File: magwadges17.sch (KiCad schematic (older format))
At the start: 23 parts, among them J1 CONN_02X03, J2 JACK_2P, Q1 BC846BDW1, Q2 BC846BDW1, U1 ATTINY2313-20MU, U2 FT25H16

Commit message: Updated schematic
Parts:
- removed D1, D2, D3, D4: LED, custom:LTST-C230KRKT, symbol LED
- removed Q1, Q2: BC846BDW1, TO_SOT_Packages_SMD:SOT-363_SC-70-6, symbol BC846BDW1
- removed R1, R2: 47, Resistors_SMD:R_0805, symbol R
- removed R3: 1K, Resistors_SMD:R_0805, symbol R
- removed R4, R5: 1M, Resistors_SMD:R_0805, symbol R
- removed R6, R7: 2K2, Resistors_SMD:R_0805, symbol R
- removed U1: ATTINY2313-20MU, Housings_DFN_QFN:QFN-20-1EP_4x4mm_Pitch0.5mm, symbol ATTINY2313-20MU
- removed U2: FT25H16, Housings_SOIC:SOIC-8_3.9x4.9mm_Pitch1.27mm, symbol FT25H16
- added RN1: R_Pack04, symbol R_Pack04
- added S5, S6, S7, S8: SW_SPST, custom:PTS645, symbol SW_SPST
- added U1: ATTINY861A-MU, QFN_MLF32, symbol ATTINY861A-MU
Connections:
- net labels added: SW_A, SW_B, SW_C, SW_D, SW_E, SW_F, SW_G, SW_H, TouchC
- wire segments 93 -> 66
- no-connect marks 8 -> 0
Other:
- moved on the sheet: J1, S1, S2, S3, S4

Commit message: Updated schematic
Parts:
- removed U1: ATTINY861A-MU, QFN_MLF32, symbol ATTINY861A-MU
- added U?: ATTINY861A-SU, Housings_SOIC:SOIC-20W_7.5x12.8mm_Pitch1.27mm, symbol ATTINY861A-SU
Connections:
- net GND: now also U?.16 (AGND), U?.6 (GND)
- net SW_A: now also U?.17 ((AREF/PCINT3)PA3)
- net SW_B: now also U?.14 ((ADC3/ICP0/PCINT4)PA4)
- net SW_C: now also U?.13 ((ADC4/AIN2/PCINT5)PA5)
- net SW_D: now also U?.12 ((ADC5/AIN0/PCINT6)PA6)
- net SW_E: now also U?.11 ((ADC6/AIN1/PCINT7)PA7)
- net SW_F: now also U?.7 ((ADC7/~OC1D~/CLKI/XTAL1/PCINT12)PB4)
- net SW_G: now also U?.8 ((ADC8/OC1D/CLKO/XTAL2/PCINT13)PB5)
- net SW_H: now also U?.9 ((ADC9/INT0/T0/PCINT14)PB6)
- net TouchA: now also U?.20 ((ADC0/DI/SDA/PCINT0)PA0)
- net TouchB: now also U?.19 ((ADC1/DO/PCINT1)PA1)
- net TouchC: now also U?.18 ((ADC2/INT1/USCK/SCL/PCINT2)PA2)
- net VCC: now also U?.15 (AVCC), U?.5 (VCC)
- net reset: now also U?.10 ((ADC10/~RESET~/PCINT15)PB7)
- net at J2.2, J2.3, LS1.1: now also U?.4 ((OC1B/PCINT11)PB3)
- net at J1.1 (P1): now also U?.2 ((MISO/DO/OC1A/PCINT9)PB1)
- net at J1.3 (P3): now also U?.3 ((SCK/USCK/SCL/~OC1B~/PCINT10)PB2)
- net at J1.4 (P4): now also U?.1 ((MOSI/DI/SDA/~OC1A~/PCINT8)PB0)
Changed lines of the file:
@@
 Wire Wire Line
 	7750 5250 7750 5200
-$Comp
-L ATTINY861A-MU U1
-U 1 1 597BCA60
-P 4050 2050
-F 0 "U1" H 3150 3000 50  0000 C CNN
-F 1 "ATTINY861A-MU" H 4750 1100 50  0000 C CNN
-F 2 "QFN_MLF32" H 4050 2050 50  0001 C CIN
-F 3 "" H 4050 2050 50  0001 C CNN
-	1    4050 2050
-	1    0    0    -1
-$EndComp
 Wire Wire Line
 	6400 3500 6350 3500
@@
 Wire Wire Line
 	7250 2050 7900 2050
+$Comp
+L ATTINY861A-SU U?
+U 1 1 597BFFA6
+P 4050 2050
+F 0 "U?" H 3150 3000 50  0000 C CNN
+F 1 "ATTINY861A-SU" H 4800 1100 50  0000 C CNN
+F 2 "Housings_SOIC:SOIC-20W_7.5x12.8mm_Pitch1.27mm" H 4050 2050 50  0001 C CIN
+F 3 "" H 4050 2050 50  0001 C CNN
+	1    4050 2050
+	1    0    0    -1
+$EndComp
 $EndSCHEMATC

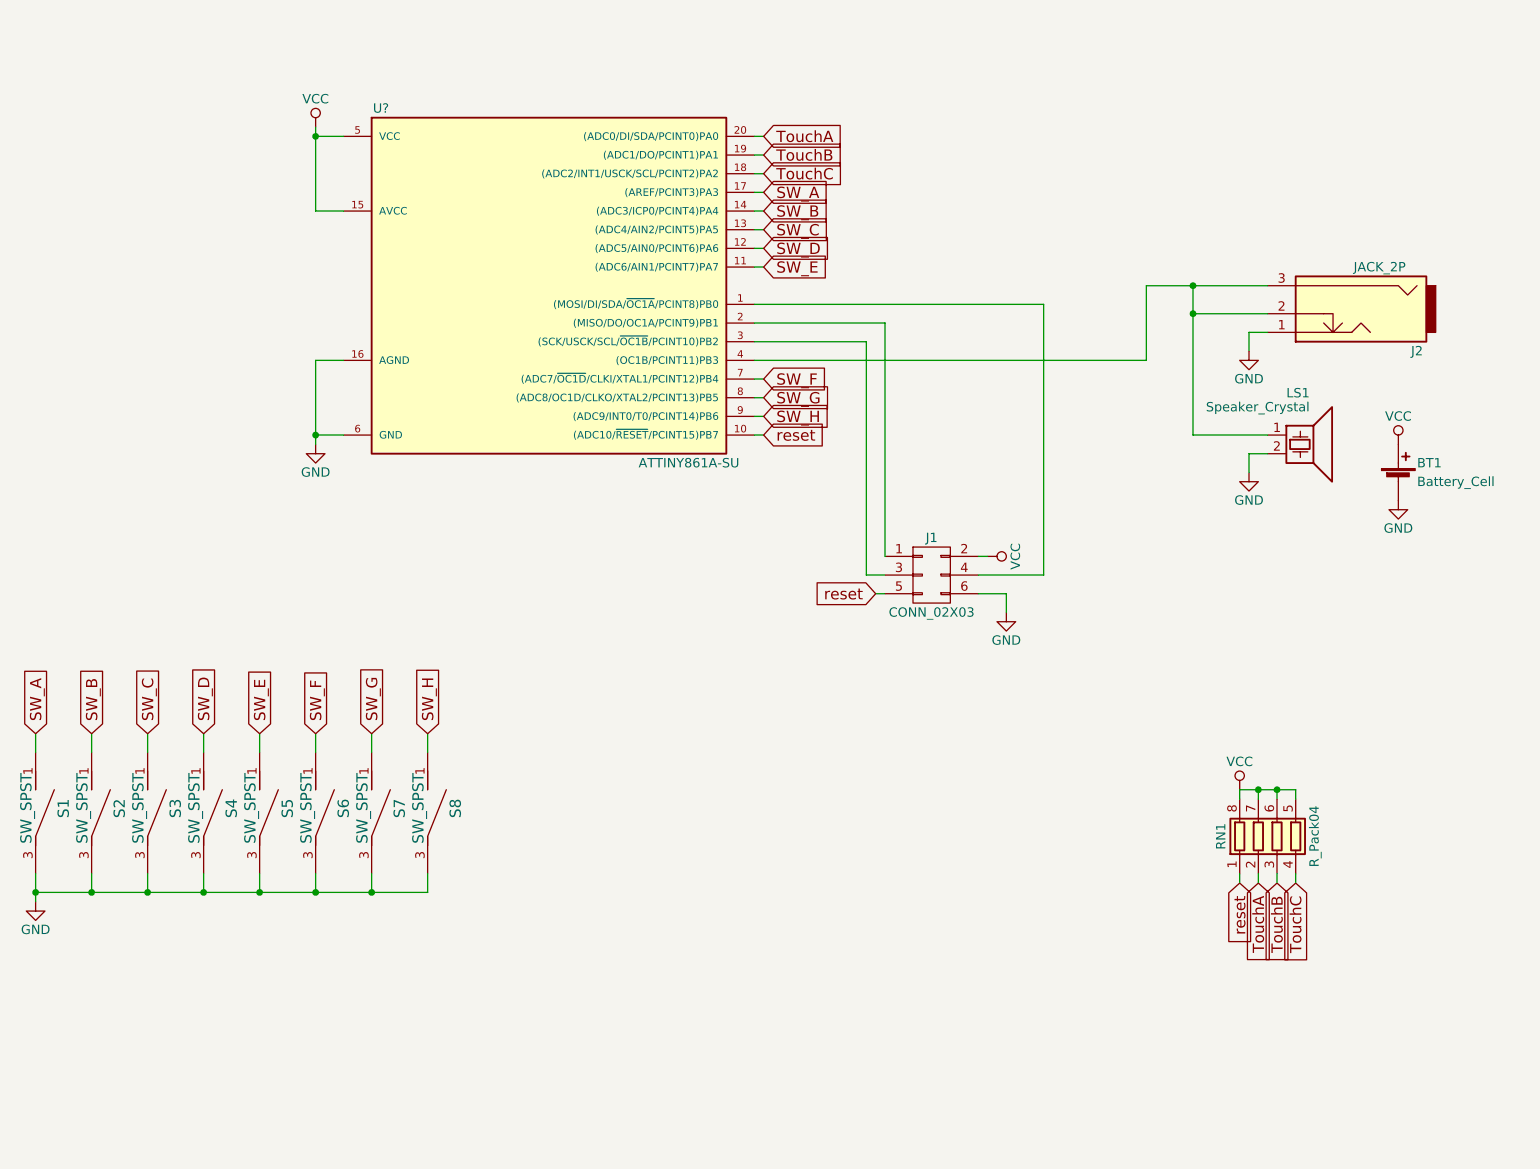
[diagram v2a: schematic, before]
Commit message: single layer in
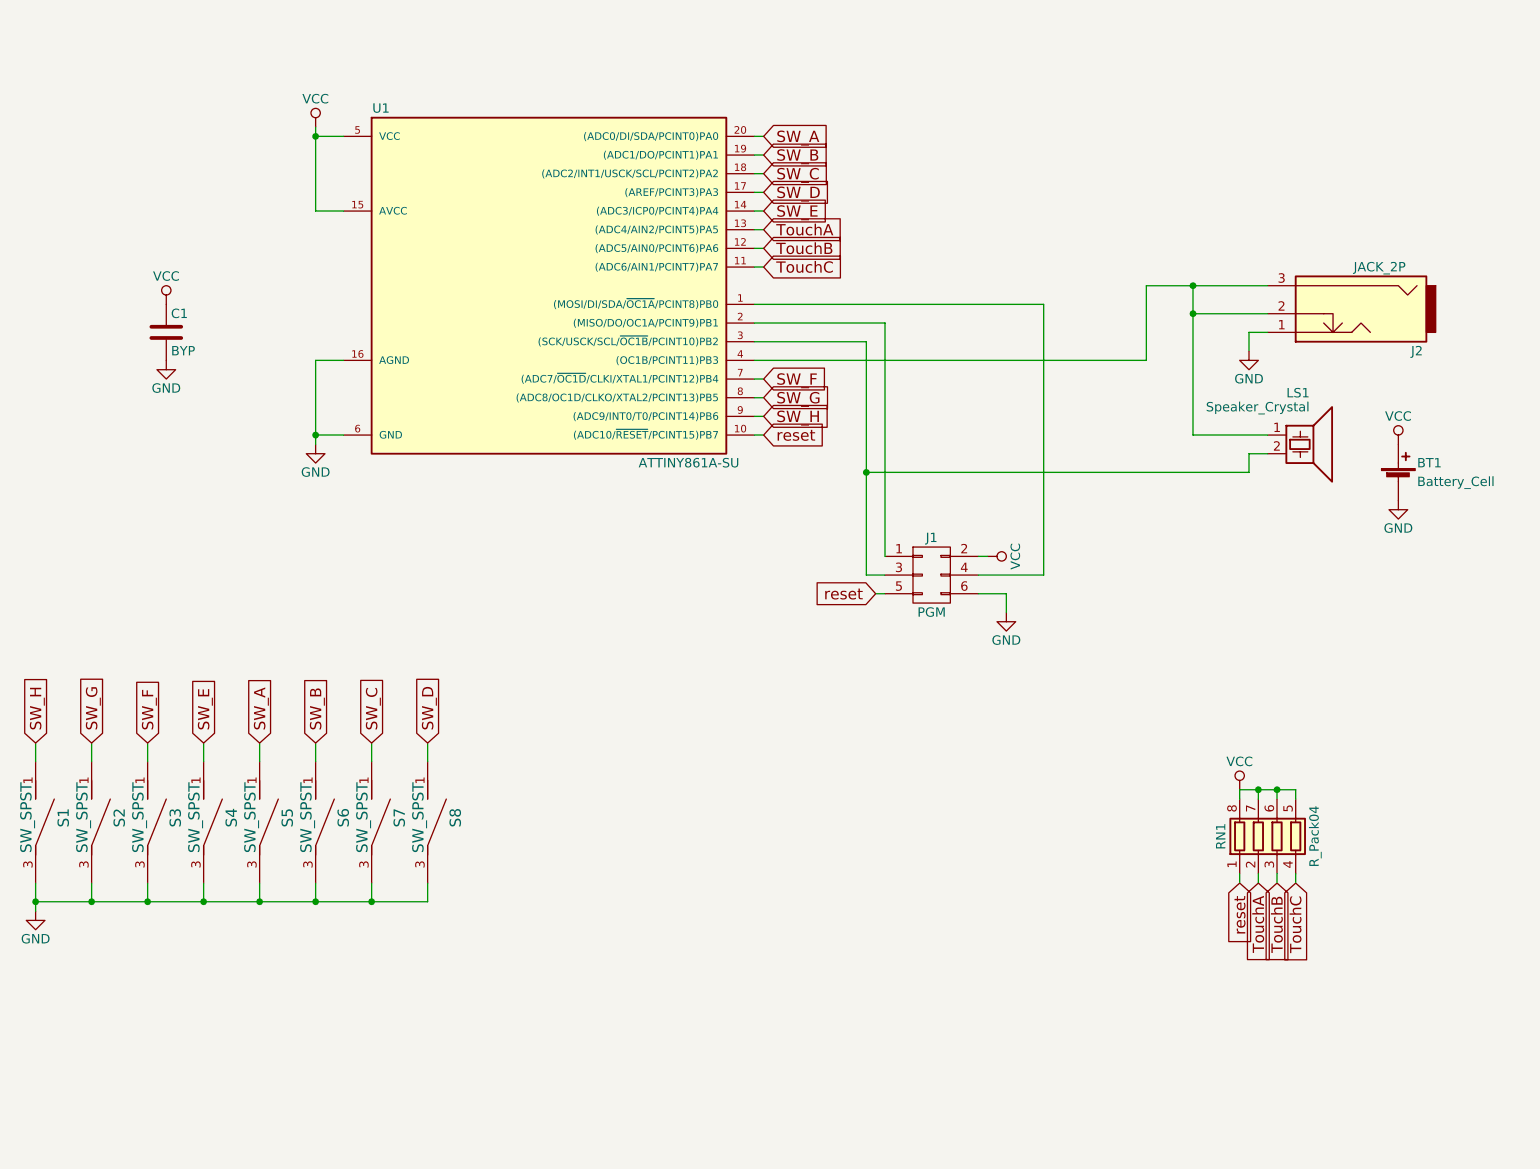
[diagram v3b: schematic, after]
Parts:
- added C1: BYP, SM0805, symbol C
- J1: value CONN_02X03 -> PGM
- RN1: footprint (none) -> NETWORK1206
- gave numbers to parts that had none: 1
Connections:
- net GND: now also C1.2; no longer LS1.2
- net SW_A: now also S5.1, U1.20 ((ADC0/DI/SDA/PCINT0)PA0); no longer S1.1, U1.17 ((AREF/PCINT3)PA3)
- net SW_B: now also S6.1, U1.19 ((ADC1/DO/PCINT1)PA1); no longer S2.1, U1.14 ((ADC3/ICP0/PCINT4)PA4)
- net SW_C: now also S7.1, U1.18 ((ADC2/INT1/USCK/SCL/PCINT2)PA2); no longer S3.1, U1.13 ((ADC4/AIN2/PCINT5)PA5)
- net SW_D: now also S8.1, U1.17 ((AREF/PCINT3)PA3); no longer S4.1, U1.12 ((ADC5/AIN0/PCINT6)PA6)
- net SW_E: now also S4.1, U1.14 ((ADC3/ICP0/PCINT4)PA4); no longer S5.1, U1.11 ((ADC6/AIN1/PCINT7)PA7)
- net SW_F: now also S3.1; no longer S6.1
- net SW_G: now also S2.1; no longer S7.1
- net SW_H: now also S1.1; no longer S8.1
- net TouchA: now also U1.13 ((ADC4/AIN2/PCINT5)PA5); no longer U1.20 ((ADC0/DI/SDA/PCINT0)PA0)
- net TouchB: now also U1.12 ((ADC5/AIN0/PCINT6)PA6); no longer U1.19 ((ADC1/DO/PCINT1)PA1)
- net TouchC: now also U1.11 ((ADC6/AIN1/PCINT7)PA7); no longer U1.18 ((ADC2/INT1/USCK/SCL/PCINT2)PA2)
- net VCC: now also C1.1
- net at J1.3 (P3), U1.3 ((SCK/USCK/SCL/~OC1B~/PCINT10)PB2): now also LS1.2
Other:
- moved on the sheet: S1, S2, S3, S4, S5, S6, S7, S8

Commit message: Update wadges
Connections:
- net SW_F: now also J1.3 (P3), U1.3 ((SCK/USCK/SCL/~OC1B~/PCINT10)PB2); no longer U1.7 ((ADC7/~OC1D~/CLKI/XTAL1/PCINT12)PB4)
- net SW_G: now also U1.4 ((OC1B/PCINT11)PB3); no longer U1.8 ((ADC8/OC1D/CLKO/XTAL2/PCINT13)PB5)
- net at J2.2, J2.3, LS1.1: now also U1.8 ((ADC8/OC1D/CLKO/XTAL2/PCINT13)PB5); no longer U1.4 ((OC1B/PCINT11)PB3)
- new net: LS1.2, U1.7 ((ADC7/~OC1D~/CLKI/XTAL1/PCINT12)PB4)
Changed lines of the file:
@@
 Text GLabel 5200 1650 2    60   Input ~ 0
 SW_E
-Text GLabel 5200 2550 2    60   Input ~ 0
+Text GLabel 5750 3200 0    60   Input ~ 0
 SW_F
-Text GLabel 5200 2650 2    60   Input ~ 0
+Text GLabel 5150 2450 2    60   Input ~ 0
 SW_G
 Text GLabel 5200 2750 2    60   Input ~ 0
@@
 	5200 1950 5150 1950
 Wire Wire Line
-	5150 2550 5200 2550
-Wire Wire Line
-	5200 2650 5150 2650
+	5150 2550 7150 2550
+Wire Wire Line
+	7250 2650 5150 2650
 Wire Wire Line
 	5150 2750 5200 2750
@@
 	5850 2250 5150 2250
 Wire Wire Line
-	5150 2450 7250 2450
-Wire Wire Line
-	7250 2450 7250 2050
+	7250 2050 7250 2650
 Wire Wire Line
 	7250 2050 7900 2050
@@
 	1    0    0    -1
 $EndComp
-Wire Wire Line
-	7800 3050 5750 3050
-Connection ~ 5750 3050
 Text GLabel 7750 5250 3    60   Input ~ 0
 reset
+Wire Wire Line
+	7150 2550 7150 3050
+Wire Wire Line
+	7150 3050 7800 3050
 $EndSCHEMATC

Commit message: Update design
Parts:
- added D1, D2, D3, D4: LED, SM0805, symbol LED
- added L1: LANYARD, 1pin, symbol CONN_01X01
- added RN2: 10k, NETWORK1206, symbol R_Pack04
- RN1: value R_Pack04 -> 1M
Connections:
- net GND: now also L1.1 (P1), RN2.5 (R4.2), RN2.6 (R3.2), RN2.7 (R2.2), RN2.8 (R1.2)
- net at J1.1 (P1), U1.2 ((MISO/DO/OC1A/PCINT9)PB1): now also D1.2 (A), D2.2 (A)
- net at J1.4 (P4), U1.1 ((MOSI/DI/SDA/~OC1A~/PCINT8)PB0): now also D3.2 (A), D4.2 (A)
- new net: D4.1 (K), RN2.4 (R4.1)
- new net: D3.1 (K), RN2.3 (R3.1)
- new net: D2.1 (K), RN2.2 (R2.1)
- new net: D1.1 (K), RN2.1 (R1.1)
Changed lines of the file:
@@
 P 7950 5000
 F 0 "RN1" V 7650 5000 50  0000 C CNN
-F 1 "R_Pack04" V 8150 5000 50  0000 C CNN
+F 1 "1M" V 8150 5000 50  0000 C CNN
 F 2 "NETWORK1206" V 8225 5000 50  0001 C CNN
 F 3 "" H 7950 5000 50  0001 C CNN
@@
 	5150 2150 6700 2150
 Wire Wire Line
-	6700 2150 6700 3600
+	6700 2050 6700 3600
 Wire Wire Line
 	6700 3600 6350 3600
@@
 	5750 3600 5850 3600
 Wire Wire Line
-	5850 2250 5150 2250
+	5150 2250 6050 2250
 Wire Wire Line
 	7250 2050 7250 2650
@@
 Wire Wire Line
 	7150 3050 7800 3050
+$Comp
+L CONN_01X01 L1
+U 1 1 5982C11E
+P 9050 4300
+F 0 "L1" H 9050 4400 50  0000 C CNN
+F 1 "LANYARD" V 9150 4300 50  0000 C CNN
+F 2 "1pin" H 9050 4300 50  0001 C CNN
+F 3 "" H 9050 4300 50  0001 C CNN
+	1    9050 4300
+	1    0    0    -1
+$EndComp
+Wire Wire Line
+	5750 2250 5750 2050
+Connection ~ 5750 2250
+Wire Wire Line
+	6050 2250 6050 2050
+Connection ~ 5850 2250
+Wire Wire Line
+	6350 2050 6350 2150
+Connection ~ 6350 2150
+Connection ~ 6700 2150
+$Comp
+L R_Pack04 RN2
+U 1 1 5982CF21
+P 6200 1250
+F 0 "RN2" V 5900 1250 50  0000 C CNN
+F 1 "10k" V 6400 1250 50  0000 C CNN
+F 2 "NETWORK1206" V 6475 1250 50  0001 C CNN
+F 3 "" H 6200 1250 50  0001 C CNN
+	1    6200 1250
+	1    0    0    -1
+$EndComp
+Wire Wire Line
+	6700 1550 6700 1750
+Wire Wire Line
+	6300 1550 6700 1550
+Wire Wire Line
+	6300 1450 6300 1550
+Wire Wire Line
+	6350 1650 6350 1750
+Wire Wire Line
+	6200 1650 6350 1650
+Wire Wire Line
+	6200 1450 6200 1650
+Wire Wire Line
+	6050 1650 6050 1750
+Wire Wire Line
+	6100 1650 6050 1650
+Wire Wire Line
+	6100 1450 6100 1650
+Wire Wire Line
+	5750 1550 5750 1750
+Wire Wire Line
+	6000 1550 5750 1550
+Wire Wire Line
+	6000 1450 6000 1550
+$Comp
+L LED D4
+U 1 1 5982C740
+P 6700 1900
+F 0 "D4" H 6700 2000 50  0000 C CNN
+F 1 "LED" H 6700 1800 50  0000 C CNN
+F 2 "SM0805" H 6700 1900 50  0001 C CNN
+F 3 "" H 6700 1900 50  0001 C CNN
+	1    6700 1900
+	0    1    1    0
+$EndComp
+$Comp
+L LED D3
+U 1 1 5982C999
+P 6350 1900
+F 0 "D3" H 6350 2000 50  0000 C CNN
+F 1 "LED" H 6350 1800 50  0000 C CNN
+F 2 "SM0805" H 6350 1900 50  0001 C CNN
+F 3 "" H 6350 1900 50  0001 C CNN
+	1    6350 1900
+	0    1    1    0
+$EndComp
+$Comp
+L LED D2
+U 1 1 5982C9EB
+P 6050 1900
+F 0 "D2" H 6050 2000 50  0000 C CNN
+F 1 "LED" H 6050 1800 50  0000 C CNN
+F 2 "SM0805" H 6050 1900 50  0001 C CNN
+F 3 "" H 6050 1900 50  0001 C CNN
+	1    6050 1900
+	0    1    1    0
+$EndComp
+$Comp
+L LED D1
+U 1 1 5982CA40
+P 5750 1900
+F 0 "D1" H 5750 2000 50  0000 C CNN
+F 1 "LED" H 5750 1800 50  0000 C CNN
+F 2 "SM0805" H 5750 1900 50  0001 C CNN
+F 3 "" H 5750 1900 50  0001 C CNN
+	1    5750 1900
+	0    1    1    0
+$EndComp
+Wire Wire Line
+	6000 800  6000 1050
+Wire Wire Line
+	6000 900  6300 900
+Wire Wire Line
+	6300 900  6300 1050
+Wire Wire Line
+	6200 1050 6200 900
+Connection ~ 6200 900
+Wire Wire Line
+	6100 900  6100 1050
+Connection ~ 6100 900
+Connection ~ 6000 900
+$Comp
+L GND #PWR012
+U 1 1 5982DE9F
+P 6000 800
+F 0 "#PWR012" H 6000 550 50  0001 C CNN
+F 1 "GND" H 6000 650 50  0000 C CNN
+F 2 "" H 6000 800 50  0001 C CNN
+F 3 "" H 6000 800 50  0001 C CNN
+	1    6000 800
+	-1   0    0    1
+$EndComp
+$Comp
+L GND #PWR013
+U 1 1 5982E2EC
+P 8850 4300
+F 0 "#PWR013" H 8850 4050 50  0001 C CNN
+F 1 "GND" H 8850 4150 50  0000 C CNN
+F 2 "" H 8850 4300 50  0001 C CNN
+F 3 "" H 8850 4300 50  0001 C CNN
+	1    8850 4300
+	1    0    0    -1
+$EndComp
 $EndSCHEMATC
